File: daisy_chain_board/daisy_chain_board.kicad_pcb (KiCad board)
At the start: 2 copper layers, 65 x 21.2 mm, 9 parts, among them J7 Conn_02x25_Odd_Even, J8 CONFLY DB25, X1 Mac, X2 Dogcow, X3 Mac2, X4 Raspberry Pi, X7 Pi

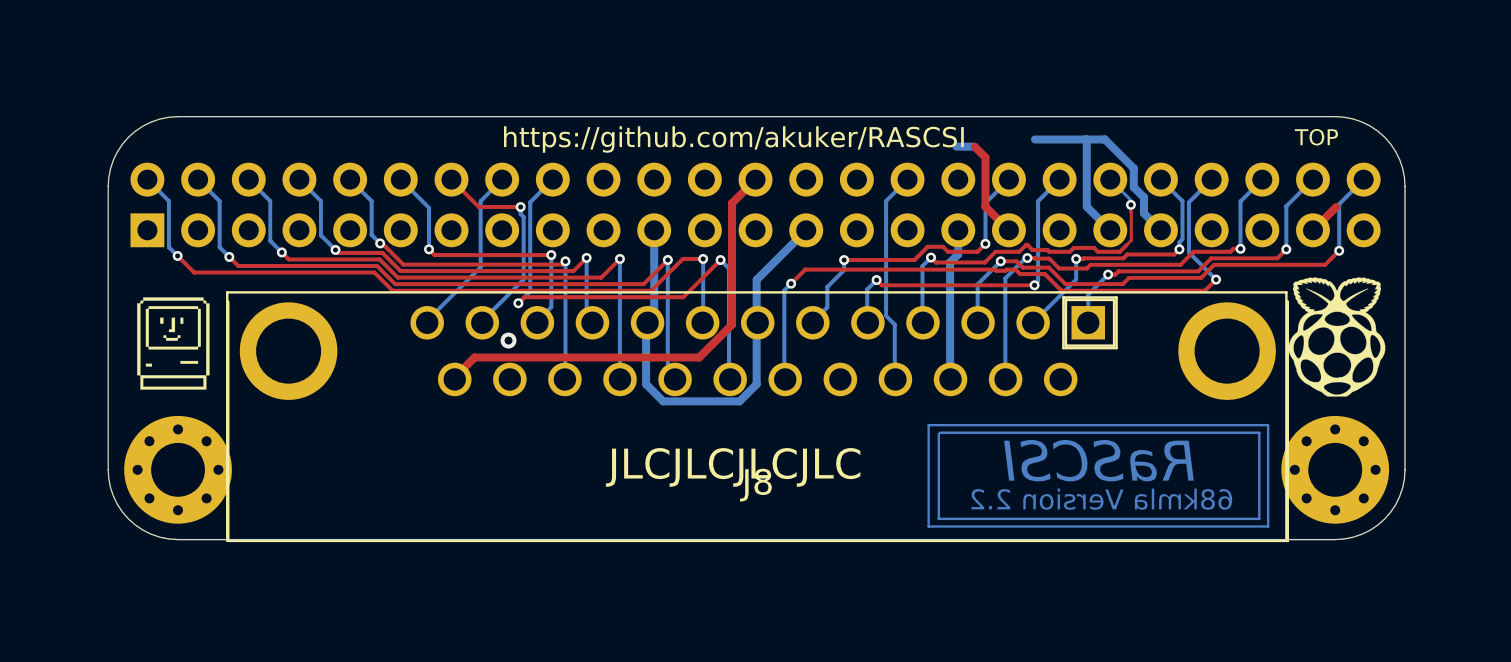
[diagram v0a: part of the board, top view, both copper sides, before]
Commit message: Fix daisychain board files (#462)
* Revert "Added STEP file and updated symbol and 3d model references to reference the correct gender of parts. Should be no functional change"

This reverts commit 479cc578b885d9d675a35aab40d5217a447c2dfc.

* Delete rascsi_tester that didn't work

Co-authored-by: Tony Kuker <akuker@gmail.com>
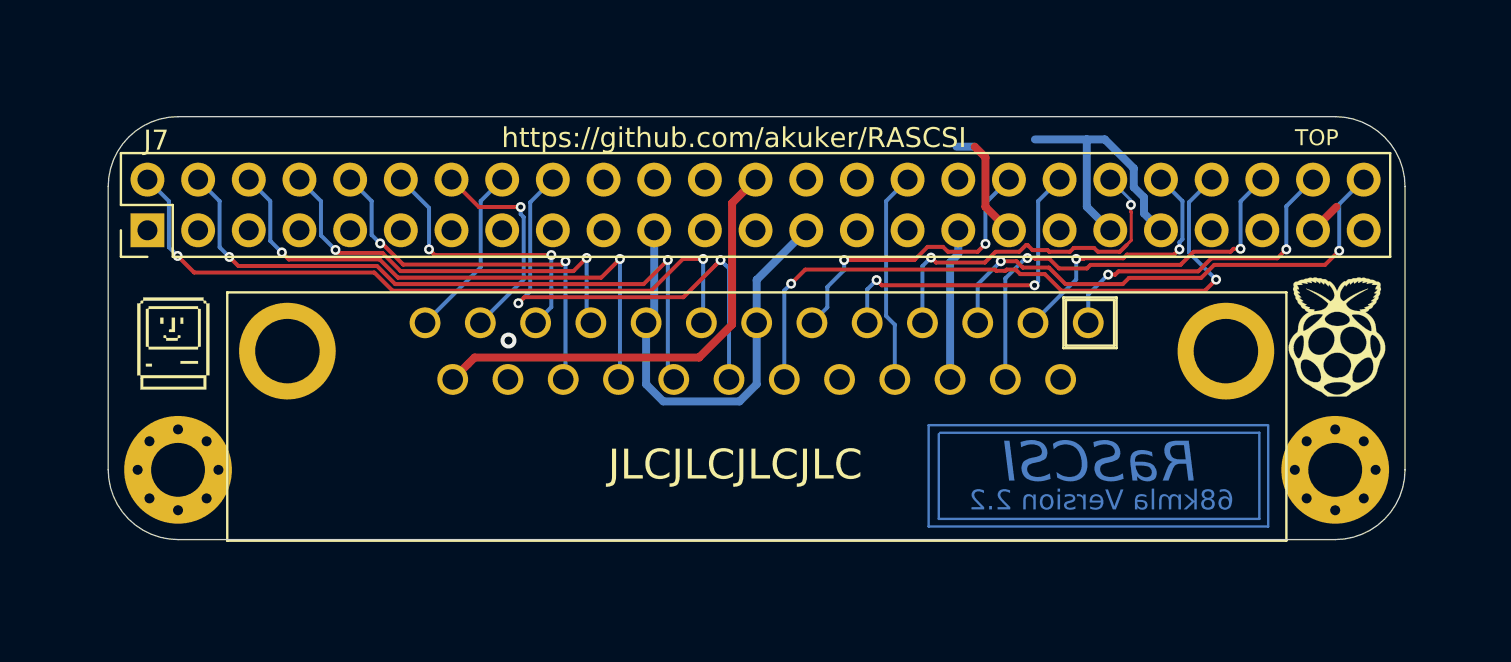
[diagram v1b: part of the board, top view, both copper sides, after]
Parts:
- J7: footprint Connector_PinSocket_2.54mm:PinSocket_2x25_P2.54mm_Vertical -> Connector_PinHeader_2.54mm:PinHeader_2x25_P2.54mm_Vertical; moved to F.Cu
- J8: value CONFLY DB25 -> L717SDB25PA4CH4F; footprint SamacSys_Parts:57489011 -> SamacSys_Parts:L717SDB25PA4CH4F; moved to B.Cu
- turned J7 to 90 degrees
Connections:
- J7 pad 25: (no net) -> Net-(J7-Pad25)
- J7 pad 34: (no net) -> Net-(J7-Pad34)

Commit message: Added STEP file and updated symbol and 3d model references to reference the correct gender of parts. Should be no functional change
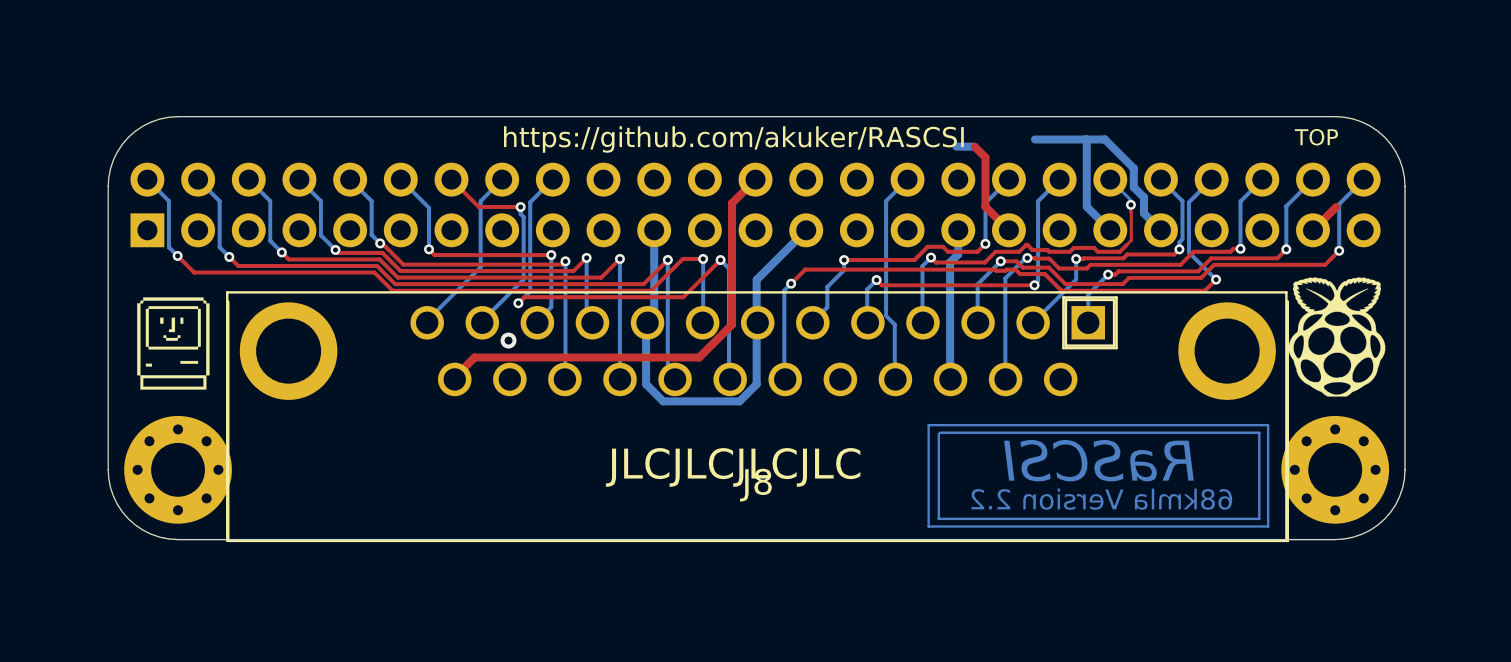
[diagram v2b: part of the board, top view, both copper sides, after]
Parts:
- J7: footprint Connector_PinHeader_2.54mm:PinHeader_2x25_P2.54mm_Vertical -> Connector_PinSocket_2.54mm:PinSocket_2x25_P2.54mm_Vertical; moved to B.Cu
- J8: value L717SDB25PA4CH4F -> CONFLY DB25; footprint SamacSys_Parts:L717SDB25PA4CH4F -> SamacSys_Parts:57489011; moved to F.Cu
- turned J7 to 270 degrees
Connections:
- J7 pad 25: Net-(J7-Pad25) -> (no net)
- J7 pad 34: Net-(J7-Pad34) -> (no net)
